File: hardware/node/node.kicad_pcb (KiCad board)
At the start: 4 copper layers, 48.5 x 50 mm, 66 parts, among them J1 BOOT0_Jumper, J2 FTDI, J3 SMA Female, J4 2 x AA, J5 SWD, Q1 Si2323DDS, SW1 DTSM-65R-V-B, U1 RFM69HW, U2 SHTC3, U3 AT25DF512C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

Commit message: Layout improvemnets
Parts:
- H1, H2, H3, H4: footprint MountingHole:MountingHole_3.2mm_M3 -> MountingHole:MountingHole_3.2mm_M3_Pad
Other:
- board text added: "OOS 2019-06-17"
- board text added: "RFM69HW Humidity Sensor"
- board text removed: "433MHz Humidity Sensor"
- board text removed: "OOS 2019-06-07"

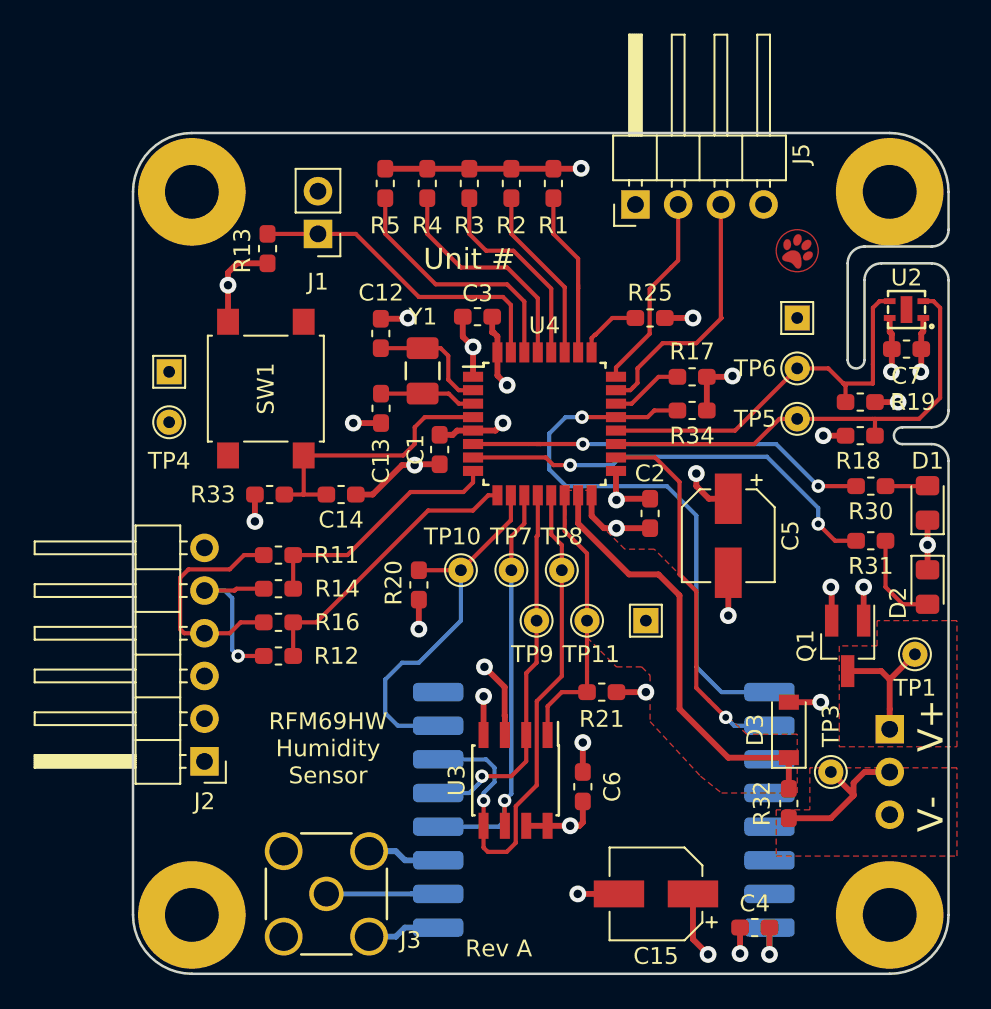
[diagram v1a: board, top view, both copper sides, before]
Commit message: Improved mounting holes and planes
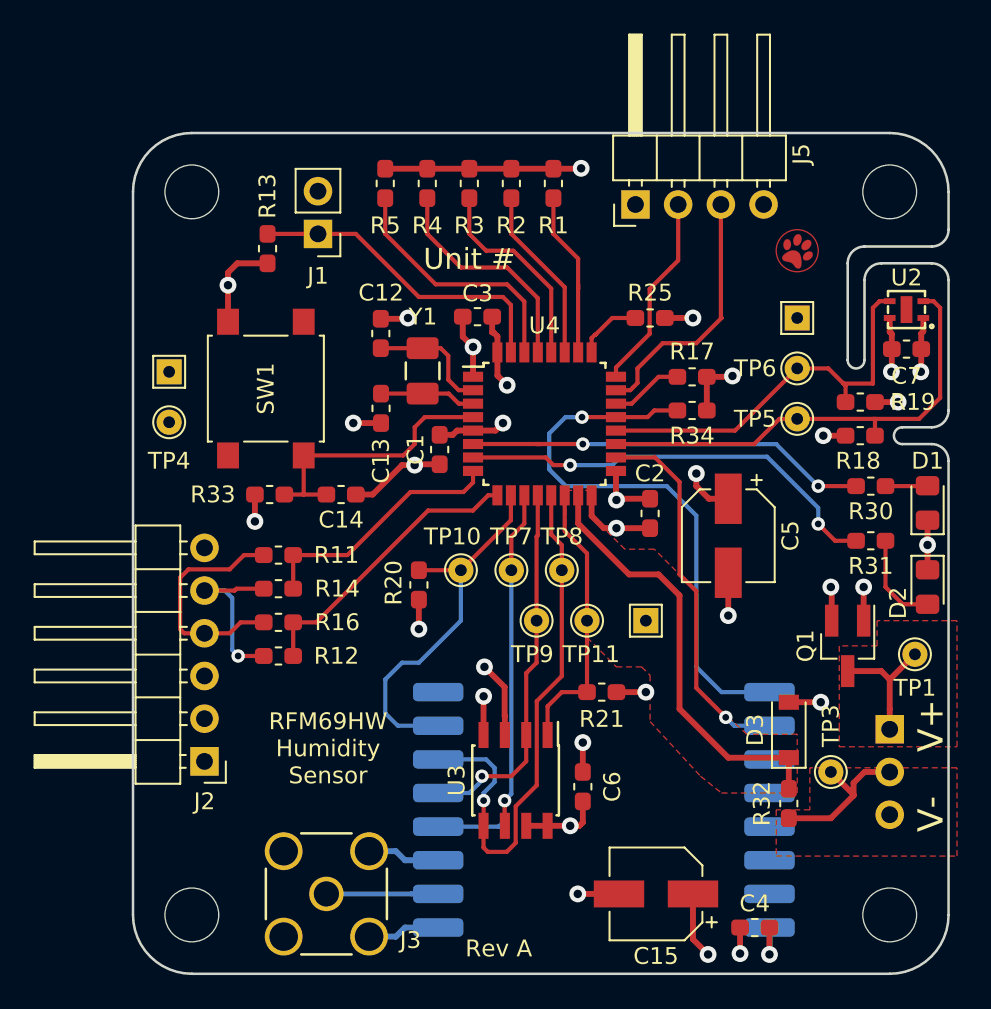
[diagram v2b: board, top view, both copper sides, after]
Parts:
- H1, H2, H3, H4: footprint MountingHole:MountingHole_3.2mm_M3_Pad -> humidity:MountingHole_3.2mm_M3

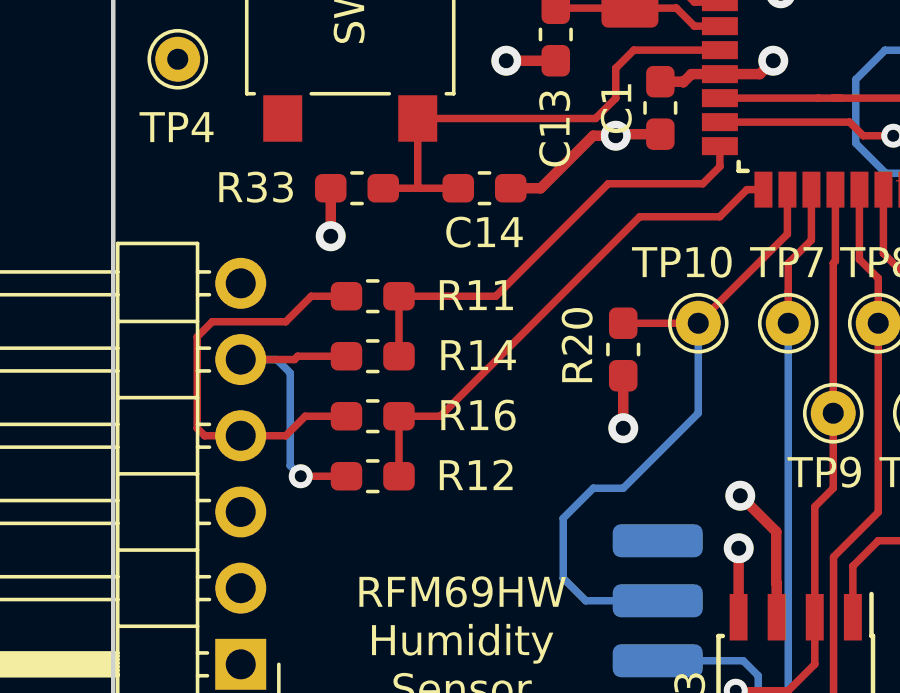
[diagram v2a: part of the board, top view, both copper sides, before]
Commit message: Improved optional resistors
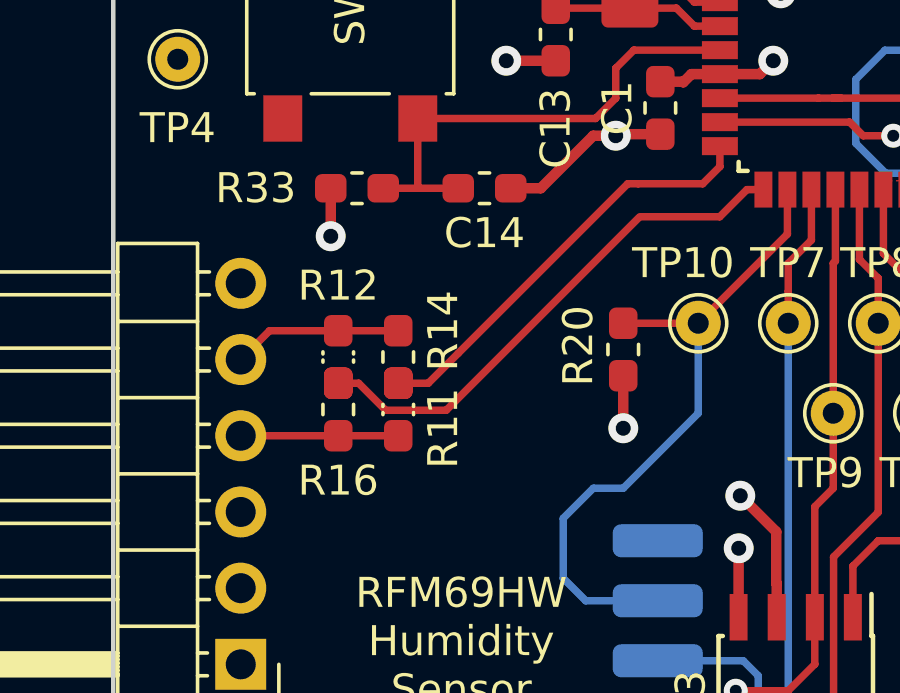
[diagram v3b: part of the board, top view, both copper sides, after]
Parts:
- moved R12 4.14 mm to (64.0, 77.1), turned to 270 degrees
- moved R11 3.87 mm to (66.0, 78.9), turned to 90 degrees
- moved R16 1.17 mm to (64.0, 78.9), turned to 90 degrees
- moved R14 0.85 mm to (66.0, 77.1), turned to 270 degrees
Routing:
- net /FTDI_TX: track 13.9 -> 5.25 mm
- net /FTDI_RX: track 10.5 -> 5.65 mm, vias 1 -> 0
- net /USART2_TX: track 15.2 -> 14.4 mm

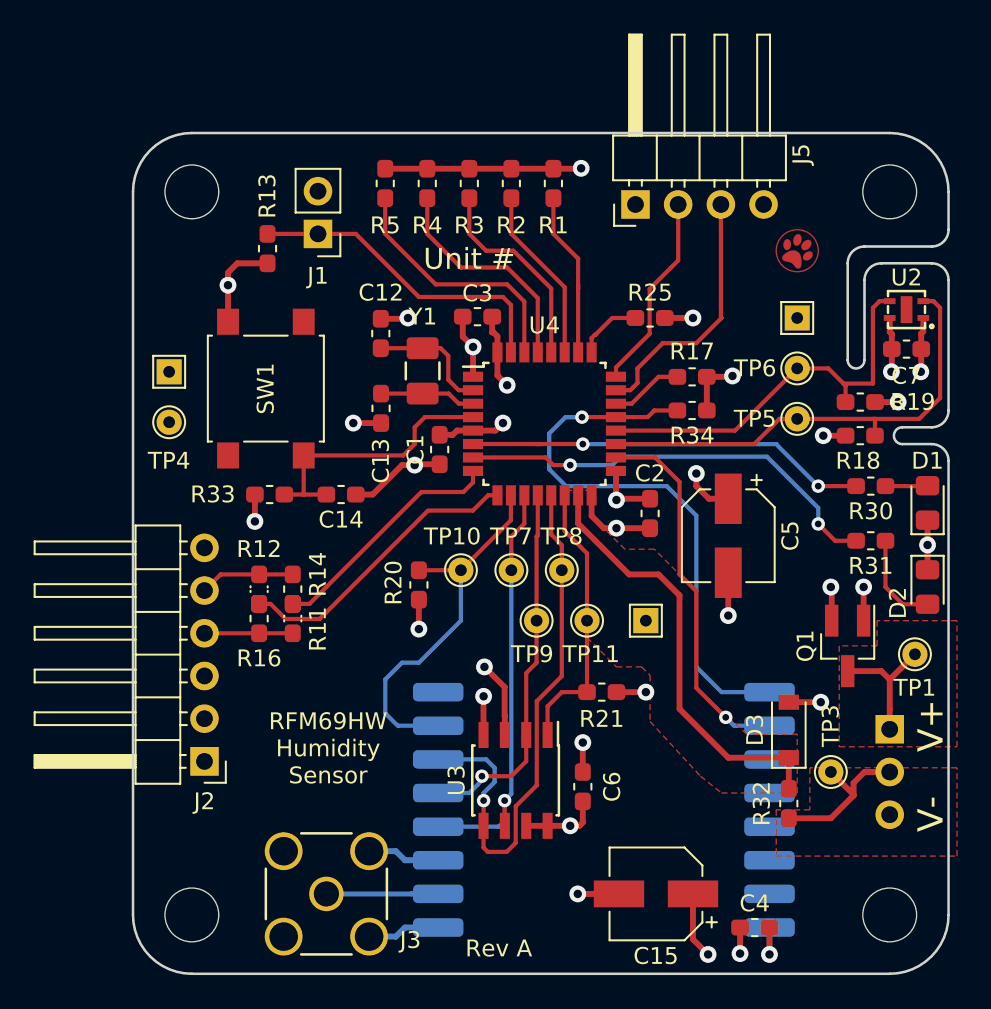
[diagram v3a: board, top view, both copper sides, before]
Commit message: DS1307 and PTH crystal
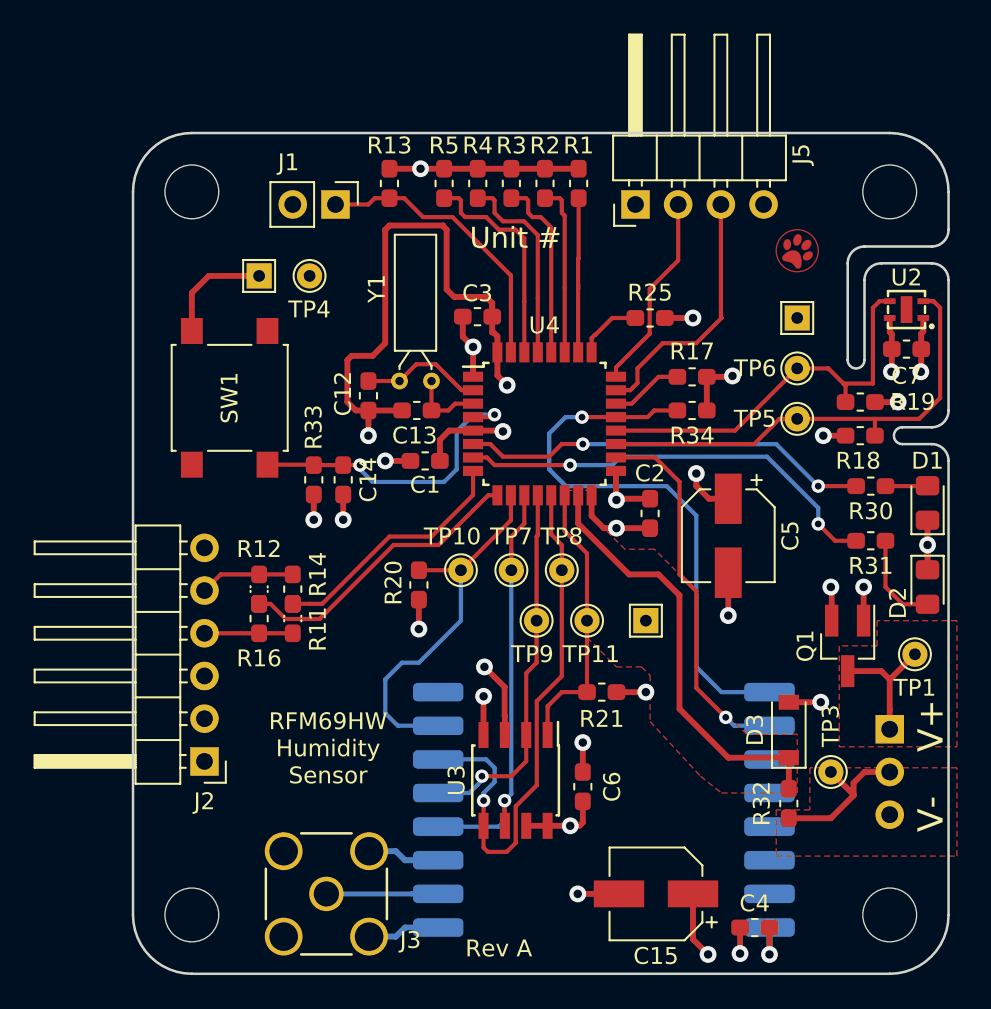
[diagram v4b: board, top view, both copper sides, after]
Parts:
- Y1: value 32.768K-CFPX217 -> 32.768K; footprint humidity:IQD_CFPX-217 -> Crystal:Crystal_C26-LF_D2.1mm_L6.5mm_Horizontal
- moved TP4 12.1 mm to (67.0, 58.5), turned to 180 degrees
- moved G*** 11.9 mm to (65.0, 67.5)
- moved R13 8.22 mm to (71.8, 53.0), turned to 90 degrees
- moved TP2 7.82 mm to (64.0, 58.5), turned to 180 degrees
- moved C12 3.77 mm to (70.5, 65.6), turned to 90 degrees
- moved R5 3.50 mm to (75.0, 53.0)
- moved R4 3.00 mm to (77.0, 53.0)
- moved R33 2.77 mm to (67.2, 70.6), turned to 90 degrees
- moved R3 2.50 mm to (79.0, 53.0)
- moved SW1 2.22 mm to (62.2, 65.8)
- moved C13 2.13 mm to (73.4, 66.5), turned to 180 degrees
- moved J1 2.04 mm to (68.5, 54.2), turned to 270 degrees
- moved R2 2.00 mm to (81.0, 53.0)
- moved R1 1.50 mm to (83.0, 53.0)
- moved C1 1.10 mm to (73.9, 69.5), turned to 0 degrees
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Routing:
- net GND: track 96.9 -> 119.9 mm, vias 18 -> 17
- net /CONF4: track 15.1 -> 13.0 mm
- net /BOOT0: track 19.0 -> 17.1 mm
- net /STM_RESET: track 16.4 -> 18.4 mm, vias 0 -> 2
- net /CONF3: track 13.5 -> 11.9 mm
- net /OSC32_OUT: track 5.72 -> 4.39 mm
- net /CONF2: track 12.1 -> 11.0 mm
- net VCC: track 44.3 -> 45.3 mm
- net /CONF0: track 10.0 -> 9.40 mm

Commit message: Minor layout adjustments
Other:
- board text added: "OOS 2019-06-24"
- board text removed: "OOS 2019-06-17"
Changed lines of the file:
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@@
   (gr_arc (start 101 58.75) (end 101 57.75) (angle -90) (layer Edge.Cuts) (width 0.15))
   (gr_line (start 104 57.75) (end 101 57.75) (layer Edge.Cuts) (width 0.15))
-  (gr_text V- (at 103.95 90.5 90) (layer F.SilkS)
+  (gr_text V- (at 103.95 90.35 90) (layer F.SilkS)
     (effects (font (size 1.5 1.5) (thickness 0.3)))
   )
-  (gr_text V+ (at 103.95 85.25 90) (layer F.SilkS)
+  (gr_text V+ (at 103.95 85.4 90) (layer F.SilkS)
     (effects (font (size 1.5 1.5) (thickness 0.3)))
   )
@@
     (effects (font (size 1.5 1.5) (thickness 0.3)) (justify mirror))
   )
-  (gr_text BOOT0 (at 67.5 51.5) (layer B.SilkS)
+  (gr_text BOOT0 (at 67.45 52) (layer B.SilkS)
     (effects (font (size 1.3 1.3) (thickness 0.25)) (justify mirror))
   )
-  (gr_text VCC (at 93.75 56 90) (layer B.SilkS)
+  (gr_text VCC (at 93.75 55.75 90) (layer B.SilkS)
     (effects (font (size 1.5 1.5) (thickness 0.3)) (justify left mirror))
   )
-  (gr_text SWDIO (at 91.46 56 90) (layer B.SilkS)
+  (gr_text SWDIO (at 91.46 55.75 90) (layer B.SilkS)
     (effects (font (size 1.5 1.5) (thickness 0.3)) (justify left mirror))
   )
-  (gr_text SWCLK (at 88.92 56 90) (layer B.SilkS)
+  (gr_text SWCLK (at 88.92 55.75 90) (layer B.SilkS)
     (effects (font (size 1.5 1.5) (thickness 0.3)) (justify left mirror))
   )
-  (gr_text GND (at 86.38 56 90) (layer B.SilkS)
+  (gr_text GND (at 86.38 55.75 90) (layer B.SilkS)
     (effects (font (size 1.5 1.5) (thickness 0.3)) (justify left mirror))
   )
@@
     (effects (font (size 1.25 1.25) (thickness 0.3)) (justify mirror))
   )
-  (gr_text "OOS 2019-06-17" (at 57.8 73.95 90) (layer B.SilkS)
+  (gr_text "OOS 2019-06-24" (at 57.8 73.95 90) (layer B.SilkS)
     (effects (font (size 1 1) (thickness 0.2)) (justify left mirror))
   )

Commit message: Slight layout adjustments
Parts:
- removed TP1, TP3: TestPoint, TestPoint:TestPoint_THTPad_D1.5mm_Drill0.7mm
- C4: moved to B.Cu
- moved TP12 9.50 mm to (77.5, 79.0)
- moved C15 4.45 mm to (92.0, 95.2)
- moved C4 3.63 mm to (97.0, 96.4), turned to 270 degrees
- moved R25 3.13 mm to (84.5, 59.5), turned to 270 degrees
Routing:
- net VCC: track 45.3 -> 47.8 mm, vias 15 -> 14
- net /V_BAT_MID: track 9.54 -> 7.14 mm
- net /V_BAT: track 7.79 -> 5.67 mm
- net /SWDIO: track 15.8 -> 14.1 mm
- net /PA15: track 3.95 -> 2.97 mm
- net /CONF3: track 11.9 -> 11.2 mm
- net /CONF4: track 13.0 -> 12.3 mm
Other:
- board text added: "OOS 2019-06-25"
- board text removed: "OOS 2019-06-24"

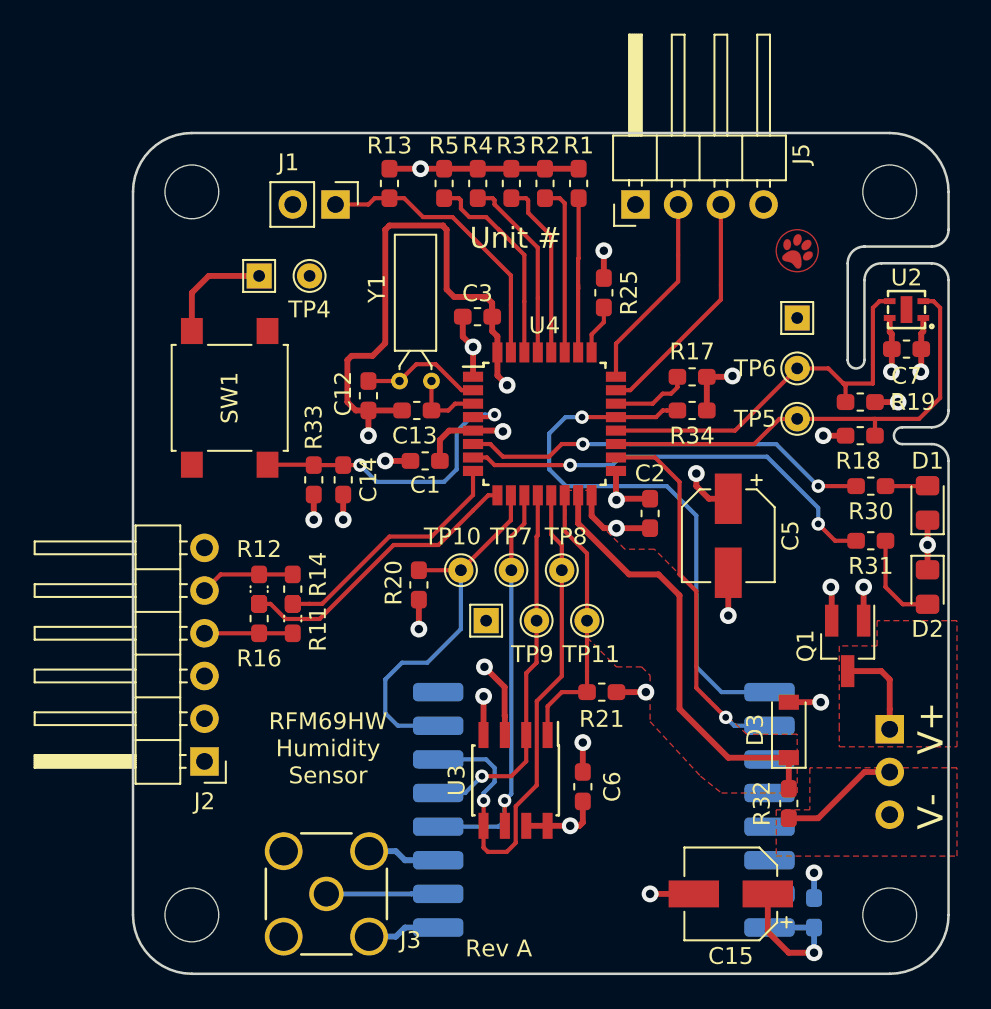
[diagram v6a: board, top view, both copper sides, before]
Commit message: Added extra decoupling
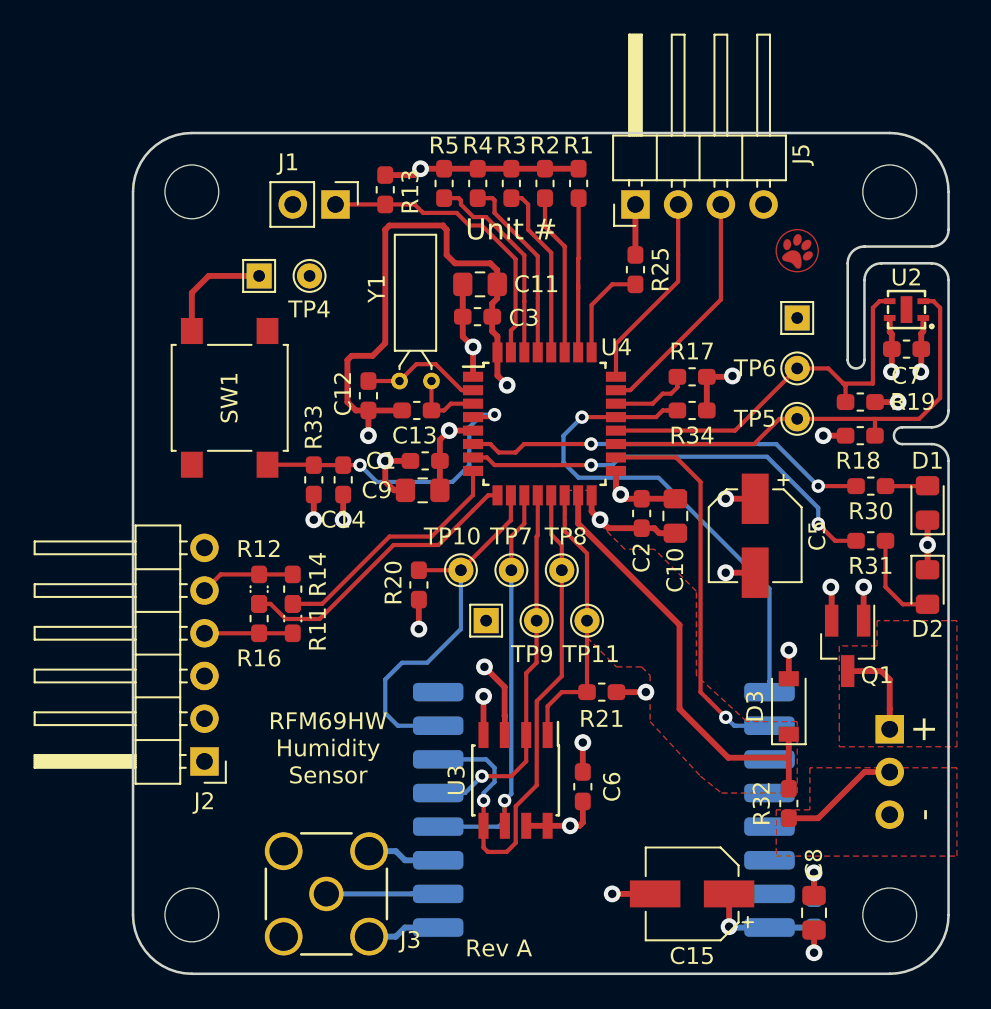
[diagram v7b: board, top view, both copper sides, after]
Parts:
- added C10: 1u, Capacitor_SMD:C_0805_2012Metric_Pad1.15x1.40mm_HandSolder, F.Cu at (88.8, 72.8)
- added C11: 1u, Capacitor_SMD:C_0805_2012Metric_Pad1.15x1.40mm_HandSolder, F.Cu at (77.1, 59.0)
- added C8: 1u, Capacitor_SMD:C_0805_2012Metric_Pad1.15x1.40mm_HandSolder, F.Cu at (97.0, 96.4)
- added C9: 1u, Capacitor_SMD:C_0805_2012Metric_Pad1.15x1.40mm_HandSolder, F.Cu at (73.7, 71.2)
- moved R25 2.33 mm to (86.4, 58.1)
- moved C15 2.30 mm to (89.8, 95.2)
- moved C5 1.60 mm to (93.5, 74.0)
- moved D3 1.40 mm to (95.5, 84.1)
- moved C2 0.50 mm to (86.8, 72.6)
- moved R13 0.45 mm to (71.5, 53.4)
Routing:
- net GND: track 119.9 -> 126.4 mm, vias 17 -> 16
- net /RFM69_RST: track 34.2 -> 30.5 mm
- net /PA15: track 2.97 -> 5.93 mm
- net VCC: track 47.8 -> 49.8 mm, vias 14 -> 15
- net /RFM69_INT: track 22.3 -> 23.1 mm
- net /BOOT0: track 17.1 -> 17.7 mm
- net /CONF1: track 10.2 -> 9.66 mm
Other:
- board text added: "+"
- board text added: "-"
- board text removed: "V+"
- board text removed: "V-"
